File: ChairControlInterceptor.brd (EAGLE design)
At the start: 80 x 53.3 mm, 14 parts, among them J1 Digital_0_7, J2 Analog, J3 Digital_8_13, SW1 TL46WO, X1 INPUT, X2 OUTPUT

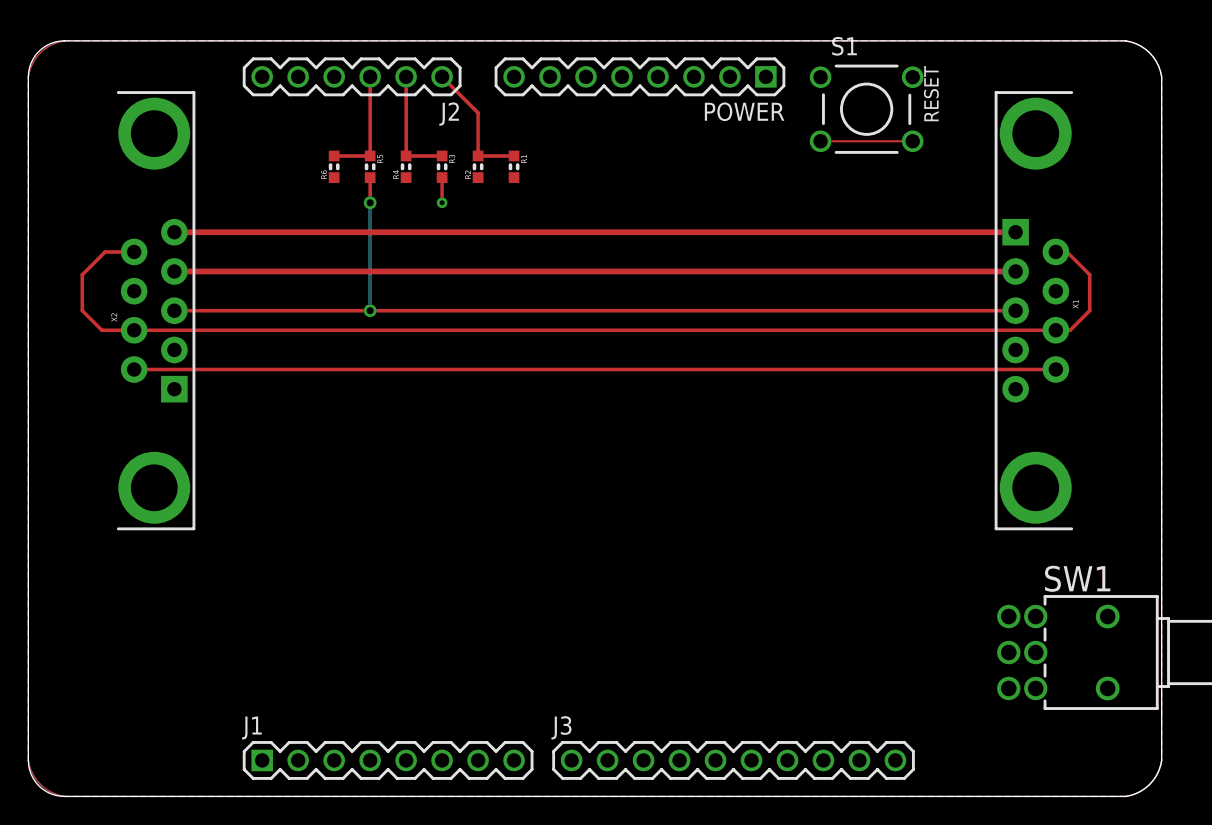
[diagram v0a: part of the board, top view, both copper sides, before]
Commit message: Added Mini DIN-4 connector for Flysky trainer cable connection
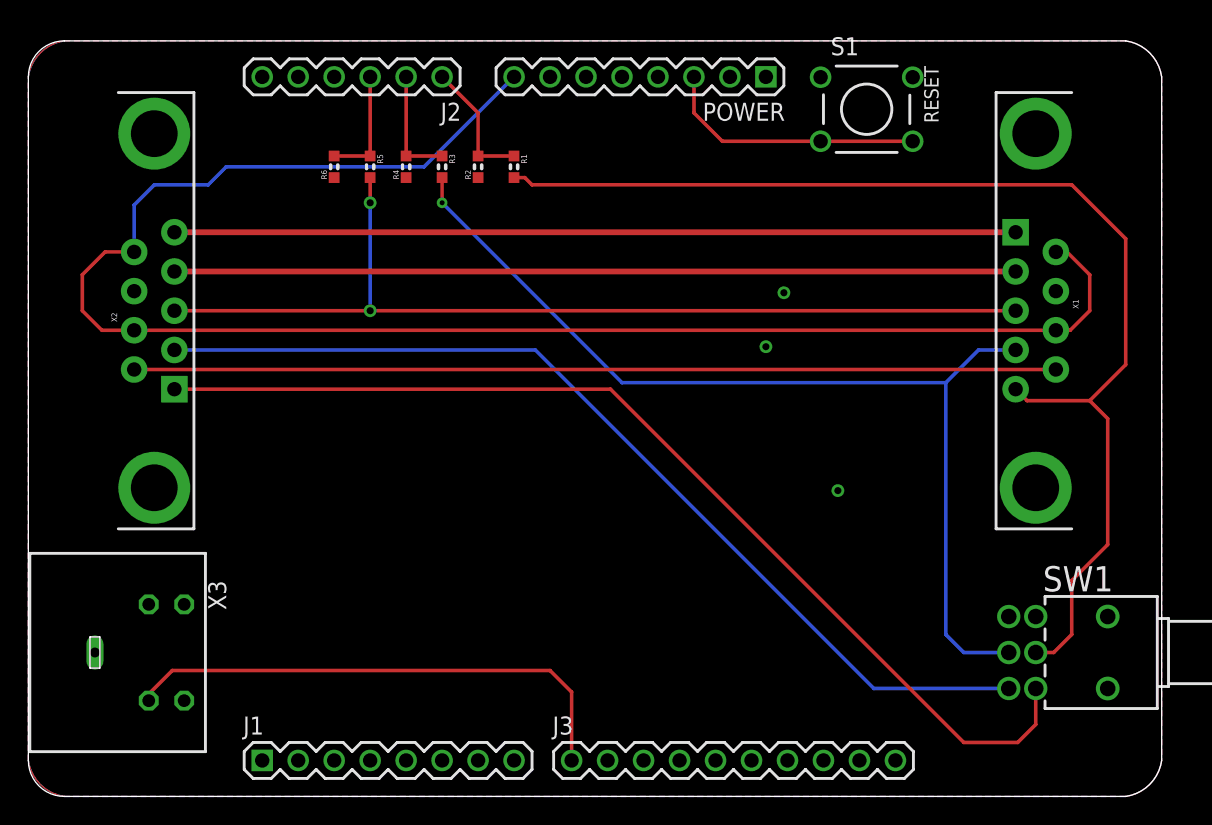
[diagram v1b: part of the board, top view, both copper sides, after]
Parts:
- added X3: (no value), freetronics-jon:MDIN04S
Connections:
- net D8: now also X3.1
- net GND: now also X3.M
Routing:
- net SPEED_IN: track 0.00 -> 84.2 mm
- net SPEED_OUT: track 0.00 -> 74.2 mm
- net DIRECTION_IN: track 1.78 -> 71.2 mm
- net DIRECTION_OUT: track 0.00 -> 68.8 mm
- net D8: track 0.00 -> 36.5 mm
- net 12V: track 84.7 -> 118.6 mm
- net RESET: track 6.50 -> 18.8 mm
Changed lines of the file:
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@@
 <?xml version="1.0" encoding="utf-8"?>
 <!DOCTYPE eagle SYSTEM "eagle.dtd">
-<eagle version="8.5.1">
+<eagle version="8.6.0">
 <drawing>
 <settings>
@@
 <setting verticaltext="up"/>
 </settings>
-<grid distance="0.05" unitdist="inch" unit="inch" style="lines" multiple="1" display="yes" altdistance="0.005" altunitdist="inch" altunit="inch"/>
+<grid distance="1" unitdist="mm" unit="mm" style="lines" multiple="1" display="yes" altdistance="0.005" altunitdist="inch" altunit="inch"/>
 <layers>
 <layer number="1" name="Top" color="4" fill="1" visible="yes" active="yes"/>
@@
 <element name="R6" library="freetronics-jon" package="0603" value="39K 1%" x="21.59" y="44.45" rot="R90"/>
 <element name="SW1" library="switch" library_urn="urn:adsk.eagle:library:380" package="TL4XWO" package3d_urn="urn:adsk.eagle:package:27749/1" value="TL46WO" x="76.2" y="10.16" rot="R270"/>
+<element name="X3" library="freetronics-jon" package="MDIN04S" value="" x="0" y="10.16" rot="R270">
+<attribute name="MF" value="" x="0" y="10.16" size="1.778" layer="27" rot="R270" display="off"/>
+<attribute name="MPN" value="" x="0" y="10.16" size="1.778" layer="27" rot="R270" display="off"/>
+<attribute name="OC_FARNELL" value="unknown" x="0" y="10.16" size="1.778" layer="27" rot="R270" display="off"/>
+<attribute name="OC_NEWARK" value="unknown" x="0" y="10.16" size="1.778" layer="27" rot="R270" display="off"/>
+</element>
 </elements>
 <signals>
@@
 <contactref element="S1" pad="4"/>
 <contactref element="POWER" pad="3"/>
-<wire x1="55.9308" y1="46.2534" x2="62.4332" y2="46.2534" width="0.1524" layer="1"/>
-<wire x1="46.99" y1="50.8" x2="62.4332" y2="46.2534" width="0" layer="19" extent="1-1"/>
+<wire x1="55.9308" y1="46.2534" x2="62.4332" y2="46.2534" width="0.254" layer="1"/>
+<wire x1="55.9308" y1="46.2534" x2="48.9966" y2="46.2534" width="0.254" layer="1"/>
+<wire x1="46.99" y1="48.26" x2="46.99" y2="50.8" width="0.254" layer="1"/>
+<wire x1="48.9966" y1="46.2534" x2="46.99" y2="48.26" width="0.254" layer="1"/>
 </signal>
 <signal name="AREF">
@@
 <signal name="D8">
 <contactref element="J3" pad="1"/>
+<contactref element="X3" pad="1"/>
+<wire x1="8.5" y1="6.76" x2="8.5" y2="7.23" width="0.254" layer="1"/>
+<wire x1="8.5" y1="7.23" x2="10.16" y2="8.89" width="0.254" layer="1"/>
+<wire x1="10.16" y1="8.89" x2="36.83" y2="8.89" width="0.254" layer="1"/>
+<wire x1="36.83" y1="8.89" x2="38.354" y2="7.366" width="0.254" layer="1"/>
+<wire x1="38.354" y1="7.366" x2="38.354" y2="2.54" width="0.254" layer="1"/>
 </signal>
 <signal name="D7">
@@
 <contactref element="R4" pad="1"/>
 <contactref element="R6" pad="1"/>
+<contactref element="X3" pad="M"/>
+<via x="57.15" y="21.59" extent="1-16" drill="0.5"/>
+<via x="53.34" y="35.56" extent="1-16" drill="0.5"/>
+<via x="52.07" y="31.75" extent="1-16" drill="0.5"/>
 </signal>
 <signal name="SDA">
@@
 <contactref element="R1" pad="2"/>
 <contactref element="SW1" pad="2"/>
-<wire x1="71.12" y1="10.16" x2="69.7" y2="28.75" width="0" layer="19" extent="1-1"/>
-<wire x1="34.29" y1="43.688" x2="71.12" y2="10.16" width="0" layer="19" extent="1-1"/>
+<wire x1="71.12" y1="10.16" x2="72.39" y2="10.16" width="0.254" layer="1"/>
+<wire x1="72.39" y1="10.16" x2="73.66" y2="11.43" width="0.254" layer="1"/>
+<wire x1="73.66" y1="11.43" x2="73.66" y2="15.24" width="0.254" layer="1"/>
+<wire x1="73.66" y1="15.24" x2="76.2" y2="17.78" width="0.254" layer="1"/>
+<wire x1="76.2" y1="17.78" x2="76.2" y2="26.67" width="0.254" layer="1"/>
+<wire x1="76.2" y1="26.67" x2="74.93" y2="27.94" width="0.254" layer="1"/>
+<wire x1="74.93" y1="27.94" x2="70.51" y2="27.94" width="0.254" layer="1"/>
+<wire x1="70.51" y1="27.94" x2="69.7" y2="28.75" width="0.254" layer="1"/>
+<wire x1="34.29" y1="43.688" x2="35.052" y2="43.688" width="0.254" layer="1"/>
+<wire x1="35.052" y1="43.688" x2="35.56" y2="43.18" width="0.254" layer="1"/>
+<wire x1="35.56" y1="43.18" x2="73.66" y2="43.18" width="0.254" layer="1"/>
+<wire x1="73.66" y1="43.18" x2="77.47" y2="39.37" width="0.254" layer="1"/>
+<wire x1="77.47" y1="30.48" x2="74.93" y2="27.94" width="0.254" layer="1"/>
+<wire x1="77.47" y1="39.37" x2="77.47" y2="30.48" width="0.254" layer="1"/>
 </signal>
 <signal name="SPEED_OUT">
 <contactref element="X2" pad="1"/>
 <contactref element="SW1" pad="3"/>
-<wire x1="10.31" y1="28.75" x2="71.12" y2="7.62" width="0" layer="19" extent="1-1"/>
+<wire x1="71.12" y1="7.62" x2="71.12" y2="5.08" width="0.254" layer="1"/>
+<wire x1="71.12" y1="5.08" x2="69.85" y2="3.81" width="0.254" layer="1"/>
+<wire x1="69.85" y1="3.81" x2="66.04" y2="3.81" width="0.254" layer="1"/>
+<wire x1="41.1" y1="28.75" x2="10.31" y2="28.75" width="0.254" layer="1"/>
+<wire x1="66.04" y1="3.81" x2="41.1" y2="28.75" width="0.254" layer="1"/>
 </signal>
 <signal name="DIRECTION_IN">
@@
 <via x="29.21" y="41.91" extent="1-16" drill="0.35"/>
 <contactref element="SW1" pad="5"/>
-<wire x1="69.215" y1="10.16" x2="69.7" y2="31.52" width="0" layer="19" extent="1-1"/>
-<wire x1="29.21" y1="41.91" x2="69.215" y2="10.16" width="0" layer="19" extent="1-1"/>
+<wire x1="69.215" y1="10.16" x2="66.04" y2="10.16" width="0.254" layer="16"/>
+<wire x1="66.04" y1="10.16" x2="64.77" y2="11.43" width="0.254" layer="16"/>
+<wire x1="64.77" y1="11.43" x2="64.77" y2="29.21" width="0.254" layer="16"/>
+<wire x1="64.77" y1="29.21" x2="67.08" y2="31.52" width="0.254" layer="16"/>
+<wire x1="67.08" y1="31.52" x2="69.7" y2="31.52" width="0.254" layer="16"/>
+<wire x1="64.77" y1="29.21" x2="41.91" y2="29.21" width="0.254" layer="16"/>
+<wire x1="41.91" y1="29.21" x2="29.21" y2="41.91" width="0.254" layer="16"/>
 </signal>
 <signal name="DIRECTION_OUT">
 <contactref element="X2" pad="2"/>
 <contactref element="SW1" pad="6"/>
-<wire x1="10.31" y1="31.52" x2="69.215" y2="7.62" width="0" layer="19" extent="1-1"/>
+<wire x1="10.31" y1="31.52" x2="35.79" y2="31.52" width="0.254" layer="16"/>
+<wire x1="59.69" y1="7.62" x2="69.215" y2="7.62" width="0.254" layer="16"/>
+<wire x1="35.79" y1="31.52" x2="59.69" y2="7.62" width="0.254" layer="16"/>
 </signal>
 <signal name="REFERENCE">
@@
 <wire x1="74.93" y1="36.83" x2="73.32" y2="38.44" width="0.254" layer="1"/>
 <wire x1="73.32" y1="38.44" x2="72.54" y2="38.44" width="0.254" layer="1"/>
-<wire x1="7.47" y1="38.44" x2="34.29" y2="50.8" width="0" layer="19" extent="1-1"/>
+<wire x1="34.29" y1="50.8" x2="27.94" y2="44.45" width="0.254" layer="16"/>
+<wire x1="13.97" y1="44.45" x2="12.7" y2="43.18" width="0.254" layer="16"/>
+<wire x1="12.7" y1="43.18" x2="8.89" y2="43.18" width="0.254" layer="16"/>
+<wire x1="8.89" y1="43.18" x2="7.47" y2="41.76" width="0.254" layer="16"/>
+<wire x1="7.47" y1="41.76" x2="7.47" y2="38.44" width="0.254" layer="16"/>
+<wire x1="27.94" y1="44.45" x2="13.97" y2="44.45" width="0.254" layer="16"/>
 </signal>
 </signals>

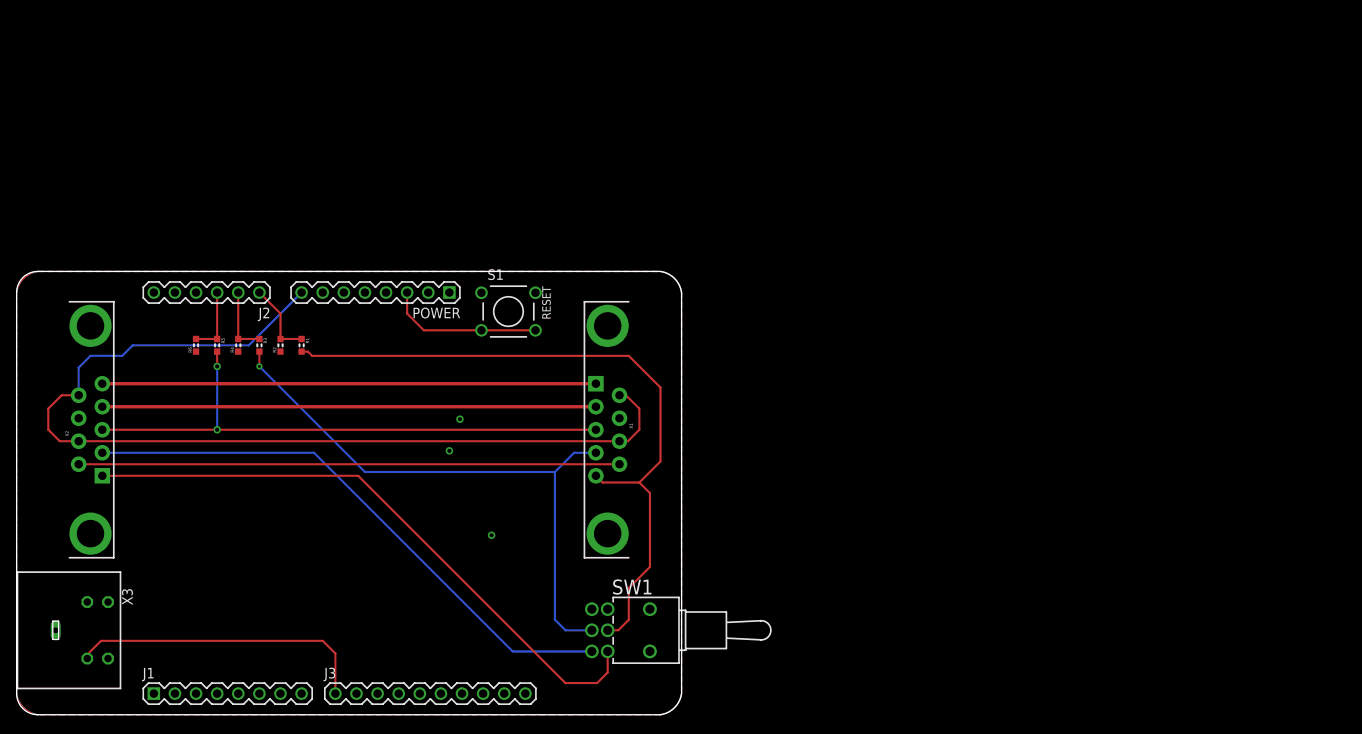
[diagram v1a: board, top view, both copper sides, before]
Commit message: Added second joystick input and changed outline to suit HB5922 case
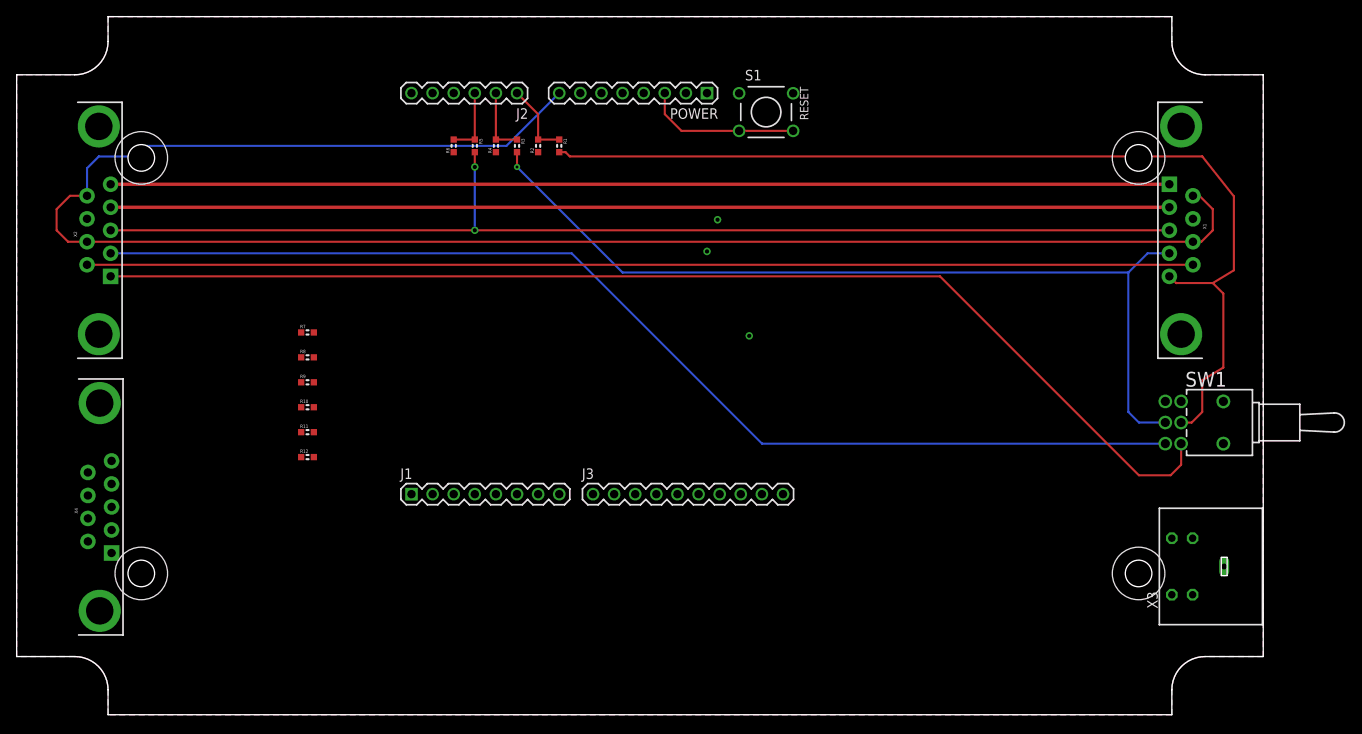
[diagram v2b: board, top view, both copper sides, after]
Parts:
- added R10, R11, R12, R7, R8, R9: 39K 1%, freetronics-jon:0603
- added X4: INPUT, SparkFun-Connectors:DB9_MALE
- moved X3 150.2 mm to (150.0, 17.8), turned to 90 degrees
- moved SW1 73.4 mm to (145.2, 35.2)
- moved X1 73.1 mm to (140.1, 58.3)
- moved R1 39.2 mm to (65.3, 68.5)
- moved J2 39.2 mm to (60.2, 74.8)
- moved J3 39.2 mm to (69.4, 26.5)
- moved R2 39.2 mm to (62.8, 68.5)
- moved R3 39.2 mm to (60.2, 68.5)
- moved R4 39.2 mm to (57.7, 68.5)
- moved R5 39.2 mm to (55.1, 68.5)
- moved R6 39.2 mm to (52.6, 68.5)
- moved S1 39.2 mm to (90.2, 72.5)
- moved J1 39.2 mm to (47.5, 26.5)
- moved POWER 39.2 mm to (83.1, 74.8)
- moved X2 24.0 mm to (9.89, 58.3)
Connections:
- new net DIRECTION_IN_2: R11.2, X4.2
- new net REFERENCE_2: R12.2, X4.3
- new net SPEED_IN_2: R7.2, X4.1
- net 12V: now also X4.7, X4.9
- net A3: now also R7.1, R8.2
- net A4: now also R11.1, R9.2
- net A5: now also R10.2, R12.1
- net GND: now also R10.1, R8.1, R9.1, X4.8
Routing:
- net 12V: track 118.6 -> 216.6 mm
- net REFERENCE: track 68.8 -> 136.8 mm
- net N$6: track 59.4 -> 127.4 mm
- net N$1: track 65.1 -> 133.1 mm
- net DETECT: track 59.4 -> 127.4 mm
- net SPEED_OUT: track 74.2 -> 141.8 mm
- net DIRECTION_OUT: track 68.8 -> 136.4 mm
- net SPEED_IN: track 84.2 -> 121.7 mm
- net DIRECTION_IN: track 71.2 -> 108.2 mm
- net D8: track 36.5 -> 0.00 mm
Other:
- board size 80 x 53.3 mm -> 150 x 84 mm

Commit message: Moved Arduino headers to correct location and adjusted connector positions
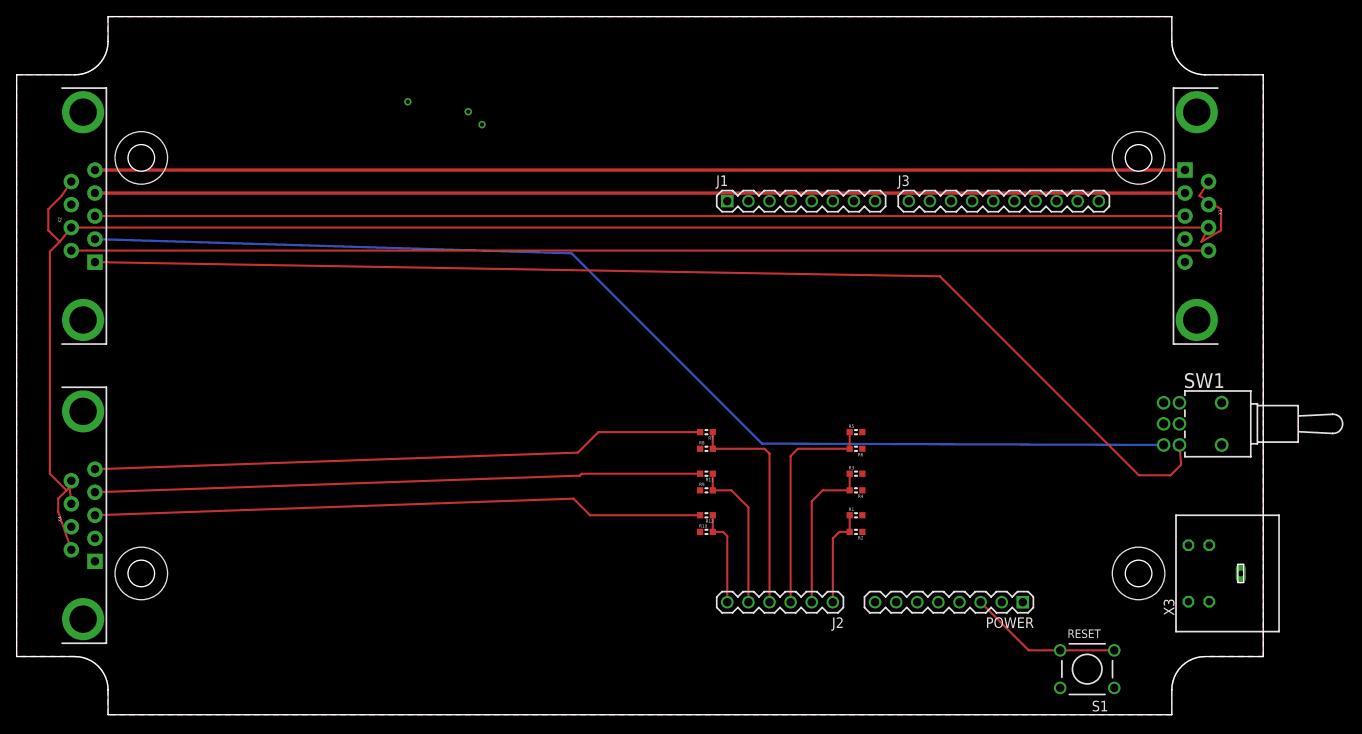
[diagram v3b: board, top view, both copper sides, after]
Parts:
- R1, R10, R11, R12, R2, R3, R4, R5, R6, R7, R8, R9: value 39K 1% -> 47K 1%
- moved S1 77.4 mm to (128.8, 5.49), turned to 180 degrees
- moved J2 72.1 mm to (98.2, 13.5)
- moved POWER 72.1 mm to (121.1, 13.5)
- moved R6 60.6 mm to (101.0, 32.0), turned to 180 degrees
- moved R2 60.2 mm to (101.0, 22.0), turned to 180 degrees
- moved R4 60.0 mm to (101.0, 27.0), turned to 180 degrees
- moved R5 57.4 mm to (101.0, 34.0), turned to 0 degrees
- moved R1 57.0 mm to (101.0, 24.0), turned to 0 degrees
- moved R3 56.7 mm to (101.0, 29.0), turned to 0 degrees
- moved J1 51.8 mm to (85.5, 61.8)
- moved J3 51.8 mm to (107.4, 61.8)
- moved R10 50.3 mm to (83.0, 22.0)
- moved R9 49.7 mm to (83.0, 27.0)
- moved R7 49.5 mm to (83.0, 34.0), turned to 180 degrees
- moved R8 49.2 mm to (83.0, 32.0)
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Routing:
- net SPEED_IN: track 121.7 -> 0.00 mm
- net DIRECTION_IN: track 108.2 -> 0.00 mm, vias 1 -> 0
- net SPEED_IN_2: track 0.00 -> 73.9 mm
- net REFERENCE_2: track 0.00 -> 73.7 mm
- net DIRECTION_IN_2: track 0.00 -> 72.9 mm
- net A3: track 0.00 -> 26.9 mm
- net A2: track 8.13 -> 27.1 mm
- net A4: track 0.00 -> 18.5 mm
- net 12V: track 216.6 -> 201.8 mm
- net A5: track 0.00 -> 11.9 mm
- net A1: track 8.13 -> 19.2 mm
- net REFERENCE: track 136.8 -> 131.2 mm, vias 2 -> 0
- net N$6: track 127.4 -> 131.2 mm
- net DETECT: track 127.4 -> 131.2 mm
- net N$1: track 133.1 -> 136.8 mm
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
